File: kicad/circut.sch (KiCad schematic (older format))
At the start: 16 parts

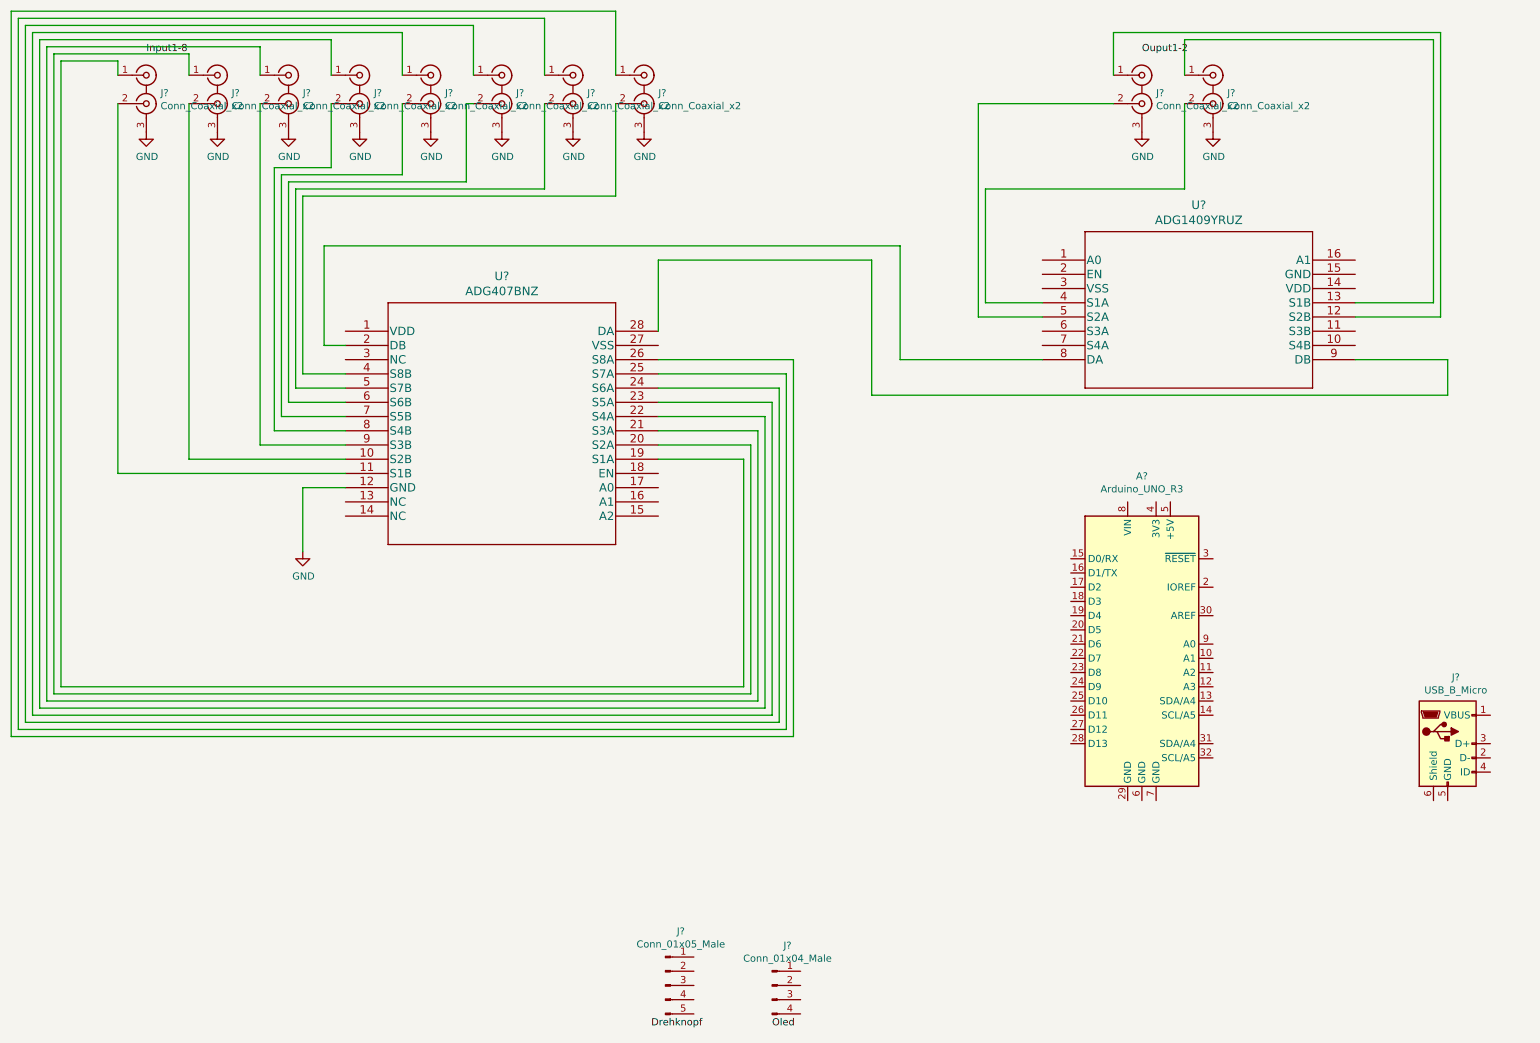
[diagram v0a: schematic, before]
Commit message: First full Wireup
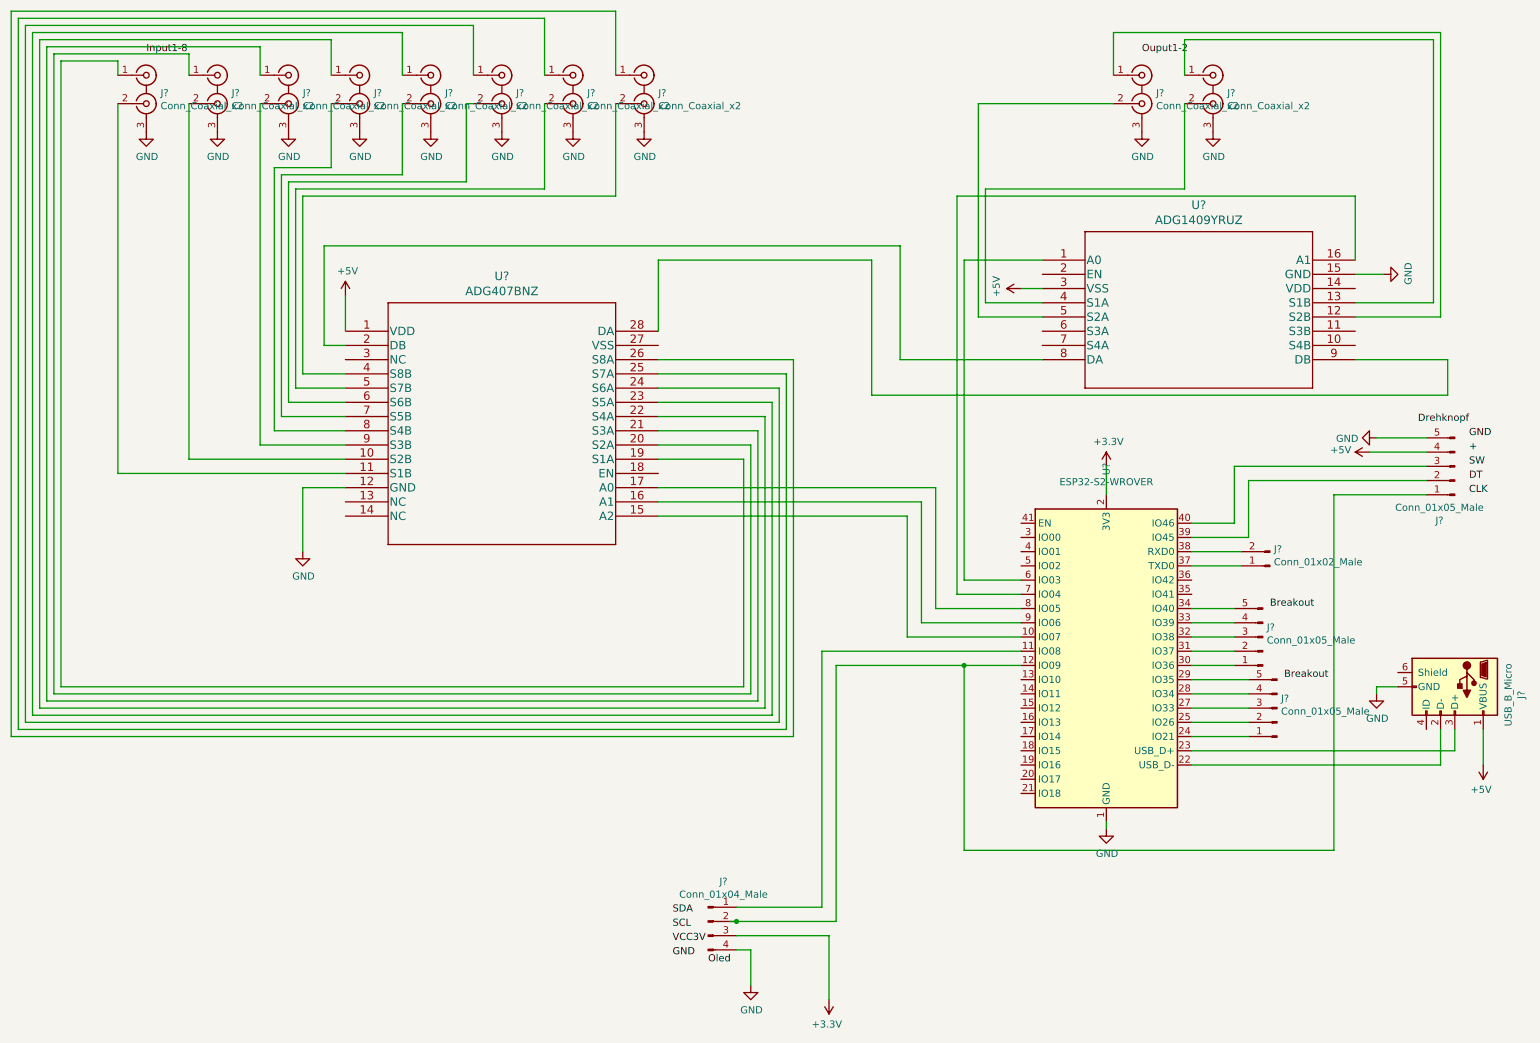
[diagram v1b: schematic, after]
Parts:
- removed A?: Arduino_UNO_R3, Module:Arduino_UNO_R3, symbol MCU_Module:Arduino_UNO_R3
- added J? (x2): Conn_01x05_Male, symbol Connector:Conn_01x05_Male
- added J?: Conn_01x02_Male, symbol Connector:Conn_01x02_Male
- added U?: ESP32-S2-WROVER, RF_Module:ESP32-S2-WROVER, symbol RF_Module:ESP32-S2-WROVER
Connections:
- net GND: now also J?.4 (Pin_4), J?.5 (GND), J?.5 (Pin_5), U?.15 (GND), U?.1 (GND), U?.26 (GND), U?.42 (GND), U?.43 (GND)
- net +5V: now reaches U?.1 (VDD)
- net +5V: now also J?.1 (VBUS), J?.4 (Pin_4), U?.3 (VSS)
- net at U?.15 (A2): now also U?.10 (IO07)
- net at U?.16 (A1): now also U?.9 (IO06)
- net at U?.17 (A0): now also U?.8 (IO05)
- net at U?.1 (A0): now also U?.6 (IO03)
- net at U?.16 (A1): now also U?.7 (IO04)
- net at J?.2 (D-): now also U?.22 (USB_D-)
- net at J?.3 (D+): now also U?.23 (USB_D+)
- net at J?.1 (Pin_1): now also U?.11 (IO08)
- net at J?.2 (Pin_2): now also J?.1 (Pin_1), U?.12 (IO09)
- net +3V3: now reaches J?.3 (Pin_3)
- net +3V3: now also U?.2 (3V3)
- net at J?.2 (Pin_2): now also U?.39 (IO45)
- net at J?.3 (Pin_3): now also U?.40 (IO46)
- new net: J?.1 (Pin_1), U?.24 (IO21)
- new net: J?.2 (Pin_2), U?.25 (IO26)
- new net: J?.3 (Pin_3), U?.27 (IO33)
- new net: J?.4 (Pin_4), U?.28 (IO34)
- new net: J?.5 (Pin_5), U?.29 (IO35)
- new net: J?.1 (Pin_1), U?.30 (IO36)
- new net: J?.2 (Pin_2), U?.31 (IO37)
- new net: J?.3 (Pin_3), U?.32 (IO38)
- new net: J?.4 (Pin_4), U?.33 (IO39)
- new net: J?.5 (Pin_5), U?.34 (IO40)
- new net: J?.1 (Pin_1), U?.37 (TXD0)
- new net: J?.2 (Pin_2), U?.38 (RXD0)
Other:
- moved on the sheet: J?

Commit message: added i2c port extender for the adgs
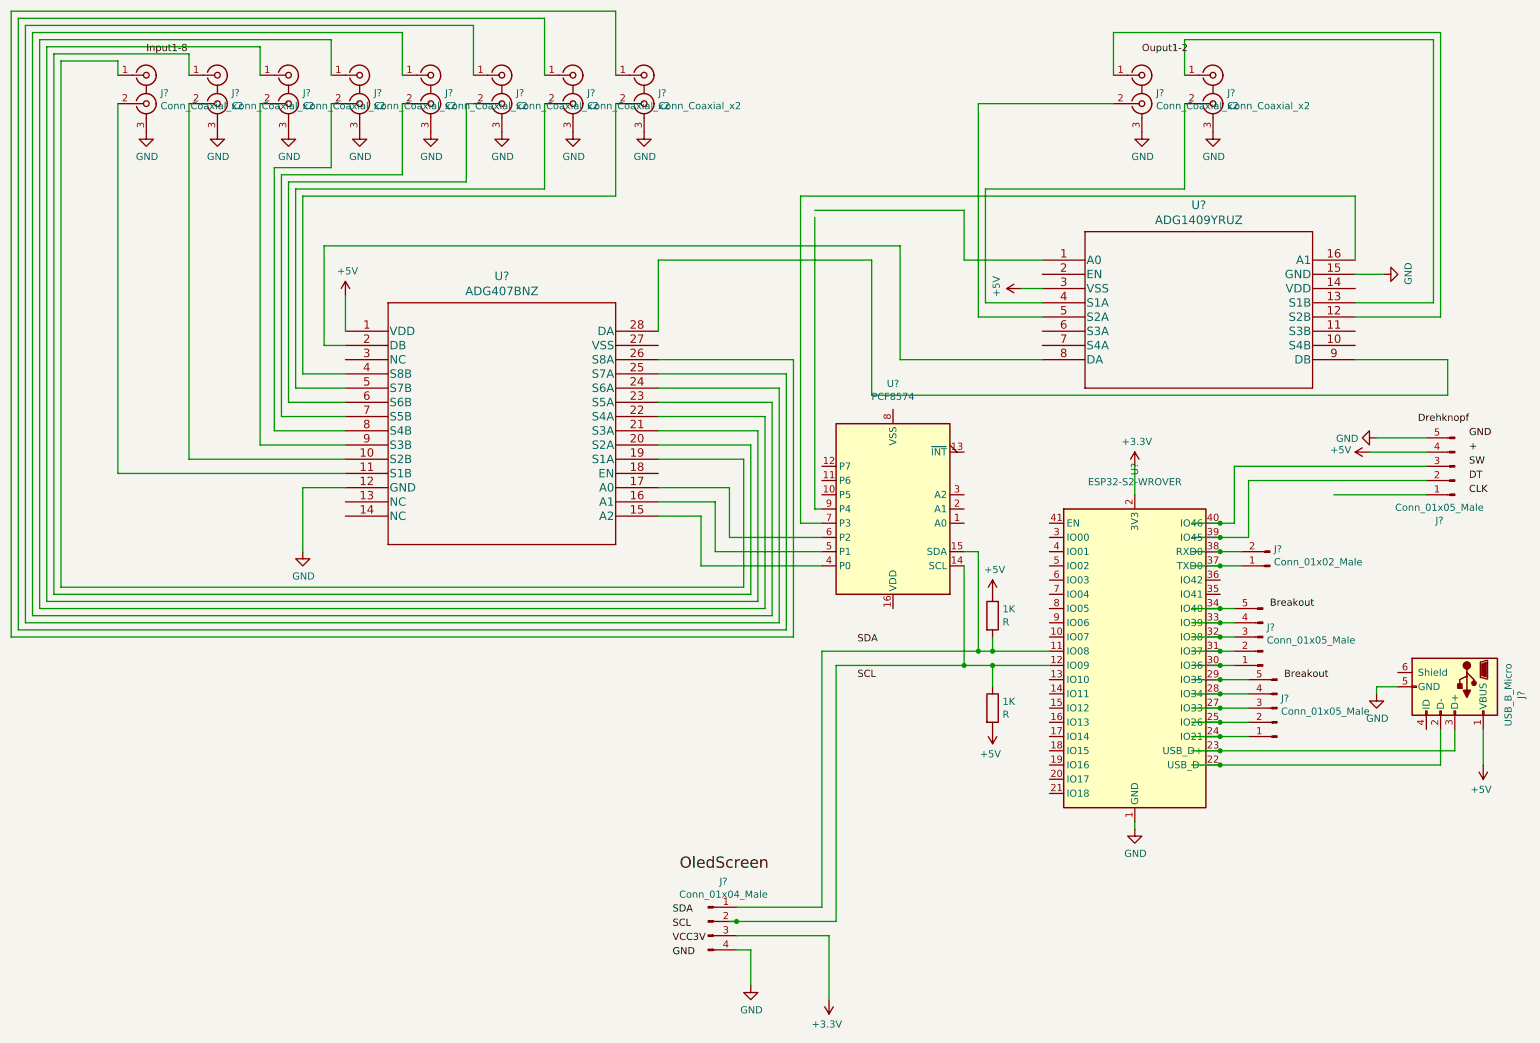
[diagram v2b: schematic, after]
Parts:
- added 1K (x2): R, symbol Device:R
- added U?: PCF8574, symbol Interface_Expansion:PCF8574
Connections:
- net labels added: OledScreen
- net labels removed: Oled
- wire segments 167 -> 190
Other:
- moved on the sheet: U?

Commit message: hating kicad
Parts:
- R1, R2: renamed from 1K; value R -> 1K
- gave numbers to parts that had none: 20
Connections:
- net labels added: 5PinBreakout1, 5PinBreakout2
- net labels removed: Breakout
